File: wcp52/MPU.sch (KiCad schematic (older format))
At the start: 56 parts, among them J6 JLINK, J8 AVR-ICSP, U12 ATSAM4S16CA-AU, U18 ATMEGA32U4-AU-DNP, X2 12MHz

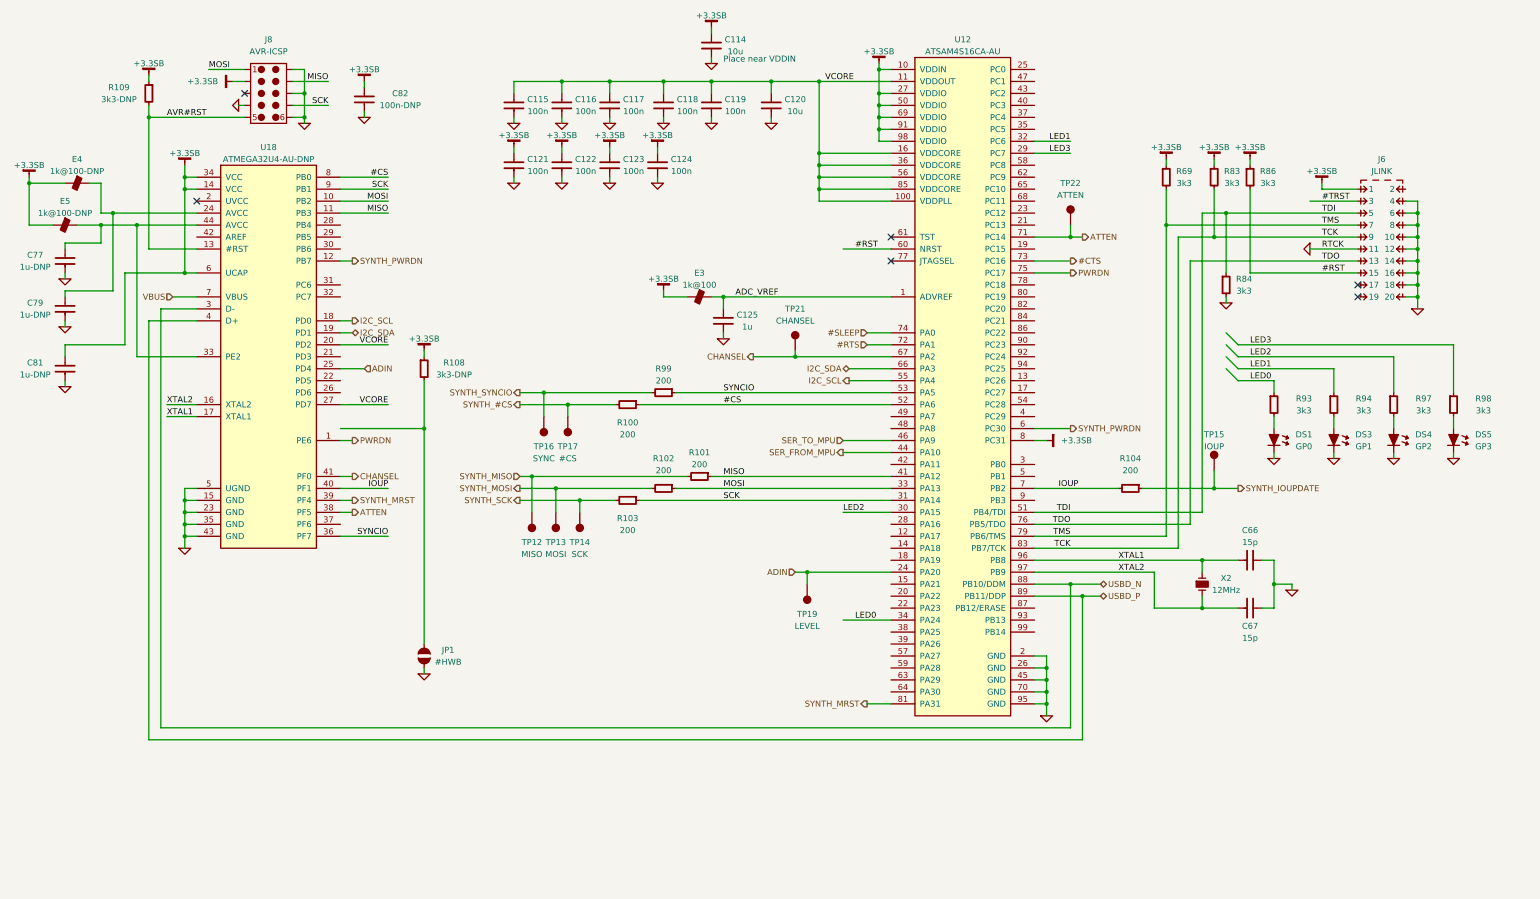
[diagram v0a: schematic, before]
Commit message: Route DDS's SDIO1 to MCUs
Just in case...
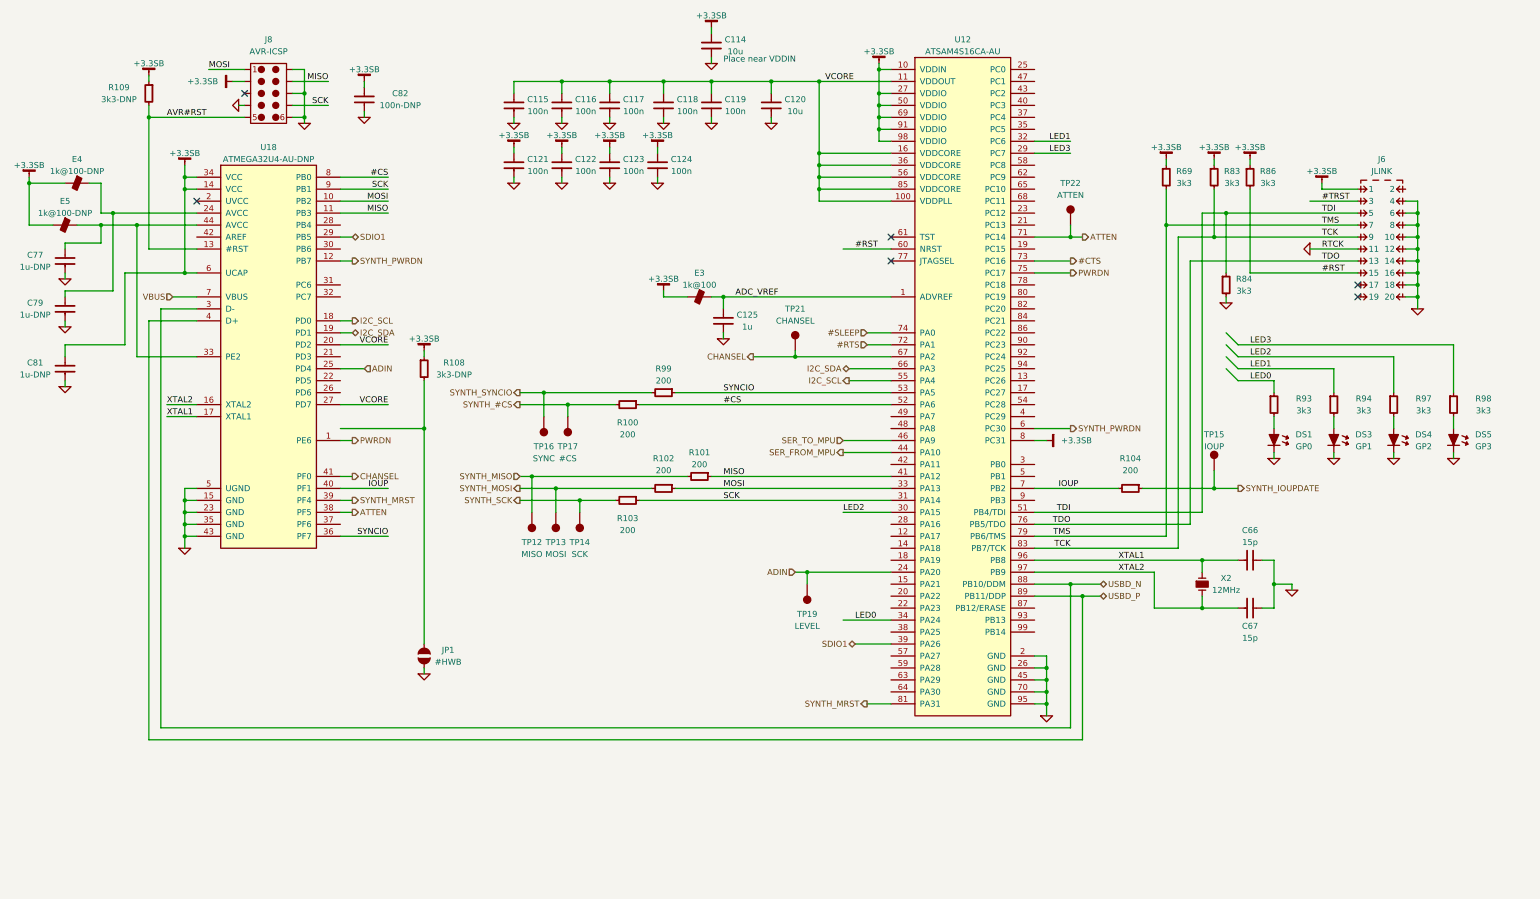
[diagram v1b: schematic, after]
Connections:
- net SDIO1: now reaches U12.39 (PA26)
- net SDIO1: now also U18.29 (PB5)
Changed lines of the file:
@@
 $EndComp
 Wire Wire Line
-	9200 6000 9200 6100
-Wire Wire Line
-	9200 6100 9200 6200
-Wire Wire Line
-	9200 6200 9200 6300
-Wire Wire Line
-	9200 6300 9200 6400
-Wire Wire Line
-	9200 6400 9200 6500
+	9200 6000 9200 6500
 Wire Wire Line
 	9200 6000 9100 6000
@@
 Connection ~ 9200 6400
 Wire Wire Line
-	4750 1200 5150 1200
-Wire Wire Line
-	5150 1200 5550 1200
-Wire Wire Line
-	5550 1200 6000 1200
-Wire Wire Line
-	6000 1200 6400 1200
-Wire Wire Line
-	6400 1200 6900 1200
-Wire Wire Line
-	6900 1200 7300 1200
-Wire Wire Line
-	7300 1200 7900 1200
-Wire Wire Line
-	7300 1200 7300 1800
-Wire Wire Line
-	7300 1800 7300 1900
-Wire Wire Line
-	7300 1900 7300 2000
-Wire Wire Line
-	7300 2000 7300 2100
-Wire Wire Line
-	7300 2100 7300 2200
+	4750 1200 7900 1200
+Wire Wire Line
+	7300 1200 7300 2200
 Wire Wire Line
 	7300 1800 7900 1800
@@
 Connection ~ 7300 2100
 Wire Wire Line
-	7800 1050 7800 1100
-Wire Wire Line
-	7800 1100 7800 1300
-Wire Wire Line
-	7800 1300 7800 1400
-Wire Wire Line
-	7800 1400 7800 1500
-Wire Wire Line
-	7800 1500 7800 1600
-Wire Wire Line
-	7800 1600 7800 1700
+	7800 1050 7800 1700
 Wire Wire Line
 	7800 1700 7900 1700
@@
 	5950 1750 5950 1800
 Wire Wire Line
-	6400 3000 6500 3000
-Wire Wire Line
-	6500 3000 7900 3000
+	6400 3000 7900 3000
 Wire Wire Line
 	6000 2950 6000 3000
@@
 	6500 3350 6500 3300
 Wire Wire Line
-	9100 5200 10500 5200
-Wire Wire Line
-	10500 5200 10800 5200
+	9100 5200 10800 5200
 Wire Wire Line
 	10500 5200 10500 5300
@@
 	10100 5300 10100 5600
 Wire Wire Line
-	10100 5600 10500 5600
-Wire Wire Line
-	10500 5600 10800 5600
+	10100 5600 10800 5600
 Wire Wire Line
 	10500 5600 10500 5500
@@
 	11000 5200 11100 5200
 Wire Wire Line
-	11100 5200 11100 5400
-Wire Wire Line
-	11100 5400 11100 5600
+	11100 5200 11100 5600
 Wire Wire Line
 	11100 5600 11000 5600
@@
 Connection ~ 11100 5400
 Wire Wire Line
-	9100 5400 9400 5400
-Wire Wire Line
-	9400 5400 9650 5400
-Wire Wire Line
-	9100 5500 9500 5500
-Wire Wire Line
-	9500 5500 9650 5500
+	9100 5400 9650 5400
+Wire Wire Line
+	9100 5500 9650 5500
 Wire Wire Line
 	9100 4800 10500 4800
@@
 	7900 4200 7500 4200
 Wire Wire Line
-	12300 2200 12300 2300
-Wire Wire Line
-	12300 2300 12300 2400
-Wire Wire Line
-	12300 2400 12300 2500
-Wire Wire Line
-	12300 2500 12300 2600
-Wire Wire Line
-	12300 2600 12300 2700
-Wire Wire Line
-	12300 2700 12300 2800
-Wire Wire Line
-	12300 2800 12300 2900
-Wire Wire Line
-	12300 2900 12300 3000
-Wire Wire Line
-	12300 3000 12300 3100
+	12300 2200 12300 3100
 Wire Wire Line
 	12300 2200 12200 2200
@@
 	11400 2200 11800 2200
 Wire Wire Line
-	10500 2300 10700 2300
-Wire Wire Line
-	10700 2300 11800 2300
+	10500 2300 11800 2300
 Wire Wire Line
 	10200 2400 11800 2400
 Wire Wire Line
-	10300 2500 10600 2500
-Wire Wire Line
-	10600 2500 11800 2500
+	10300 2500 11800 2500
 Wire Wire Line
 	11400 2600 11800 2600
@@
 	10900 2800 11800 2800
 Wire Wire Line
-	10200 2100 10200 2400
-Wire Wire Line
-	10200 2400 10200 5000
+	10200 2100 10200 5000
 Connection ~ 10200 2400
 Wire Wire Line
@@
 	10900 1850 10900 1900
 Wire Wire Line
-	4800 3900 5200 3900
-Wire Wire Line
-	5200 3900 5600 3900
-Wire Wire Line
-	10000 4600 10600 4600
-Wire Wire Line
-	10600 4600 10800 4600
+	4800 3900 5600 3900
+Wire Wire Line
+	10000 4600 10800 4600
 Wire Wire Line
 	7700 6400 7900 6400
 Wire Wire Line
-	4800 3800 5000 3800
-Wire Wire Line
-	5000 3800 5900 3800
-Wire Wire Line
-	6750 3500 7100 3500
-Wire Wire Line
-	7100 3500 7900 3500
-Wire Wire Line
-	4800 4700 5300 4700
-Wire Wire Line
-	5300 4700 5600 4700
-Wire Wire Line
-	4800 4500 4900 4500
-Wire Wire Line
-	4900 4500 6200 4500
-Wire Wire Line
-	4800 4600 5100 4600
-Wire Wire Line
-	5100 4600 5900 4600
-Wire Wire Line
-	7100 5300 7200 5300
-Wire Wire Line
-	7200 5300 7900 5300
+	4800 3800 5900 3800
+Wire Wire Line
+	6750 3500 7900 3500
+Wire Wire Line
+	4800 4700 5600 4700
+Wire Wire Line
+	4800 4500 6200 4500
+Wire Wire Line
+	4800 4600 5900 4600
+Wire Wire Line
+	7100 5300 7900 5300
 Wire Wire Line
 	7550 3600 7900 3600
@@
 Connection ~ 7200 5300
 Wire Wire Line
-	9100 2500 9400 2500
-Wire Wire Line
-	9400 2500 9500 2500
+	9100 2500 9500 2500
 Wire Wire Line
 	9400 2800 9100 2800
@@
 	2000 2100 2100 2100
 Wire Wire Line
-	2000 1900 2000 2000
-Wire Wire Line
-	2000 2000 2000 2100
-Wire Wire Line
-	2000 2100 2000 2800
+	2000 1900 2000 2800
 Wire Wire Line
 	2100 2000 2000 2000
 Connection ~ 2000 2000
 Wire Wire Line
-	1100 2400 1300 2400
-Wire Wire Line
-	1300 2400 1600 2400
-Wire Wire Line
-	1600 2400 2100 2400
+	1100 2400 2100 2400
 Wire Wire Line
 	700  2400 900  2400
 Wire Wire Line
-	700  2000 700  2050
-Wire Wire Line
-	700  2050 700  2400
+	700  2000 700  2400
 Wire Wire Line
 	1000 2050 700  2050
@@
 	1300 2050 1300 2300
 Wire Wire Line
-	1300 2300 1400 2300
-Wire Wire Line
-	1400 2300 2100 2300
+	1300 2300 2100 2300
 Wire Wire Line
 	1000 2600 1000 2550
@@
 	1500 3400 1500 2800
 Wire Wire Line
-	1500 2800 2000 2800
-Wire Wire Line
-	2000 2800 2100 2800
+	1500 2800 2100 2800
 Wire Wire Line
 	1000 3750 1000 3700
@@
 Connection ~ 9400 5400
 Wire Wire Line
-	2000 4600 2000 4700
-Wire Wire Line
-	2000 4700 2000 4800
-Wire Wire Line
-	2000 4800 2000 4900
-Wire Wire Line
-	2000 4900 2000 5000
-Wire Wire Line
-	2000 5000 2000 5100
+	2000 4600 2000 5100
 Wire Wire Line
 	2000 4600 2100 4600
@@
 	3300 4100 4000 4100
 Wire Wire Line
-	4000 3700 4000 4100
-Wire Wire Line
-	4000 4100 4000 5900
+	4000 3700 4000 5900
 $Comp
 L JUMPER-SOLDER JP1
@@
 	2500 1500 1700 1500
 Wire Wire Line
-	1700 1400 1700 1500
-Wire Wire Line
-	1700 1500 1700 2600
+	1700 1400 1700 2600
 Wire Wire Line
 	1700 2600 2100 2600
@@
 	2900 1100 3000 1100
 Wire Wire Line
-	3000 1100 3000 1300
-Wire Wire Line
-	3000 1300 3000 1500
-Wire Wire Line
-	3000 1500 3000 1550
+	3000 1100 3000 1550
 Wire Wire Line
 	2900 1500 3000 1500
@@
 Wire Wire Line
 	3500 1200 3500 1250
+Text HLabel 7600 5900 0    50   BiDi ~ 0
+SDIO1
+Wire Wire Line
+	7600 5900 7900 5900
+Text HLabel 3400 2500 2    50   BiDi ~ 0
+SDIO1
+Wire Wire Line
+	3400 2500 3300 2500
 $EndSCHEMATC

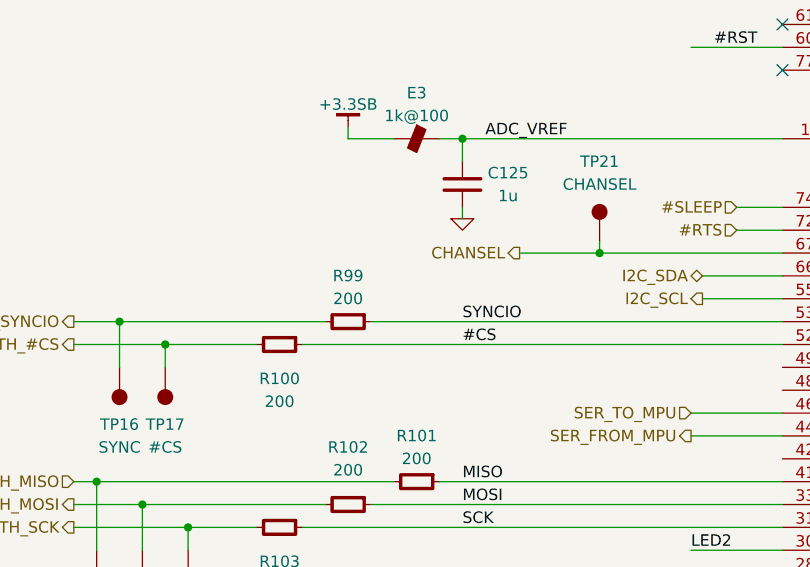
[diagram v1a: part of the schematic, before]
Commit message: Add #CS pullup resistor
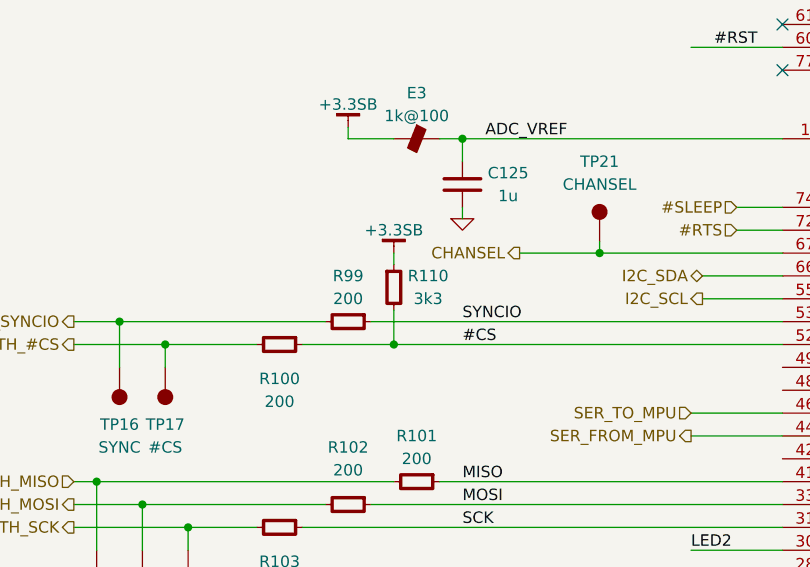
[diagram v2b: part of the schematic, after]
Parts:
- added R110: 3k3, IPC7351-Nominal:RESC1608X50, symbol R-0603
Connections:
- net #CS: now also R110.2
- net +3.3SB: now also R110.1
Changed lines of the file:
@@
 Wire Wire Line
 	3400 2500 3300 2500
+$Comp
+L R-0603 R110
+U 1 1 55011121
+P 6200 3650
+F 0 "R110" H 6350 3700 50  0000 C CNN
+F 1 "3k3" H 6350 3600 50  0000 C CNN
+F 2 "IPC7351-Nominal:RESC1608X50" H 6200 3650 50  0001 C CNN
+F 3 "" H 6200 3700 60  0000 C CNN
+F 4 "Value" H 6200 3650 60  0001 C CNN "Manuf"
+F 5 "RES SMD 3.3k 5% [0603]" H 6950 4200 60  0001 C CNN "BOM"
+	1    6200 3650
+	1    0    0    -1
+$EndComp
+Wire Wire Line
+	6200 3750 6200 3900
+Connection ~ 6200 3900
+$Comp
+L +3.3SB #PWR0265
+U 1 1 550116AB
+P 6200 3500
+F 0 "#PWR0265" H 6200 3550 30  0001 C CNN
+F 1 "+3.3SB" H 6200 3600 50  0000 C CNN
+F 2 "" H 6200 3500 60  0000 C CNN
+F 3 "" H 6200 3500 60  0000 C CNN
+	1    6200 3500
+	1    0    0    -1
+$EndComp
+Wire Wire Line
+	6200 3500 6200 3550
 $EndSCHEMATC

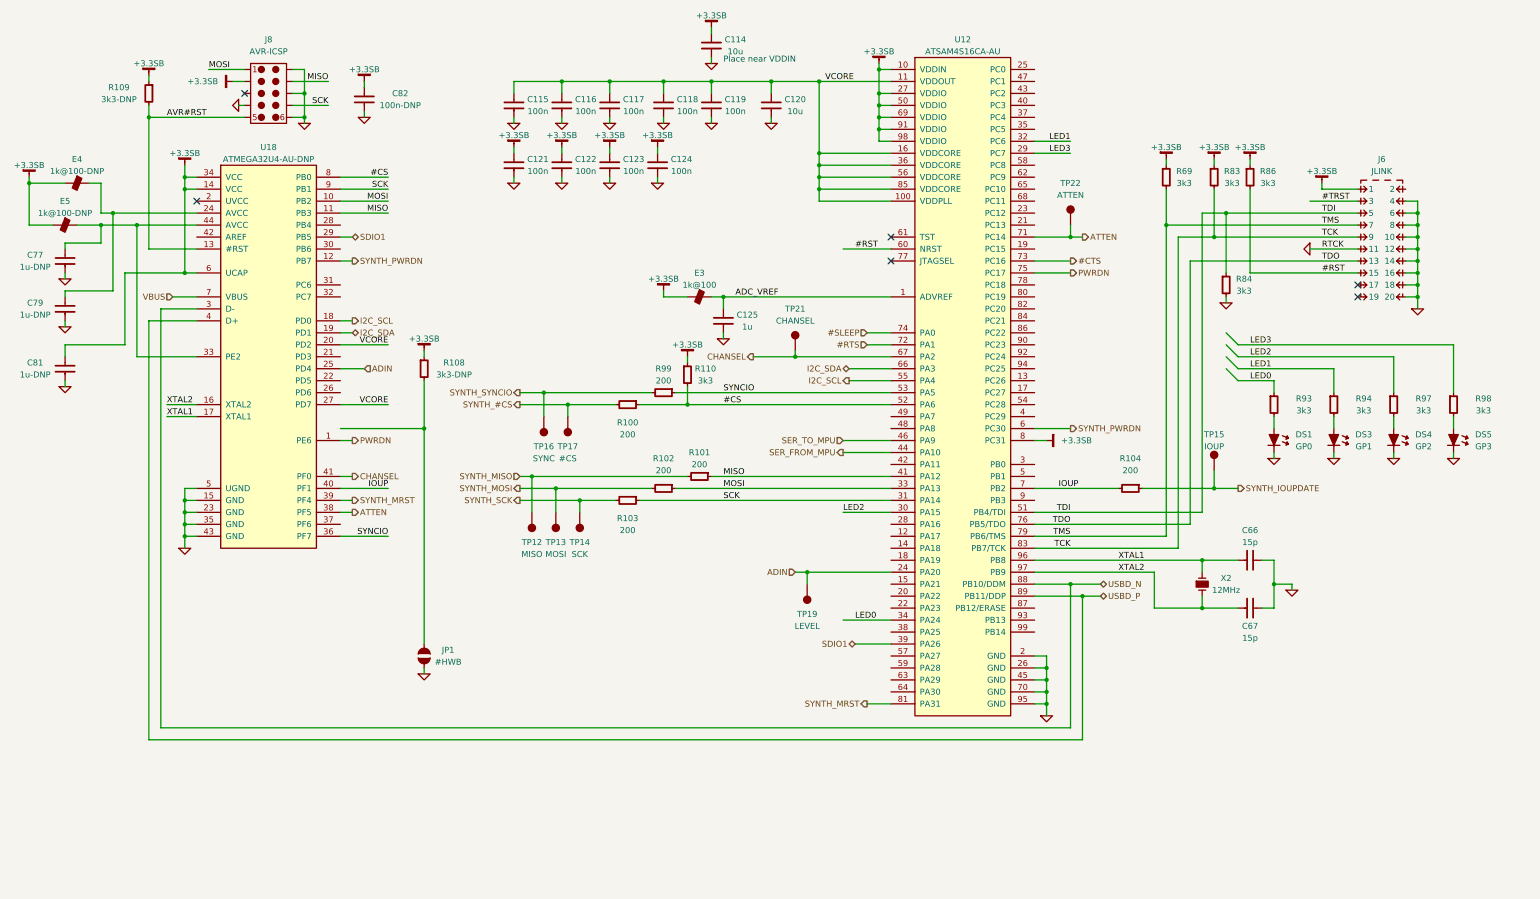
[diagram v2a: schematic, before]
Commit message: Route UART to alt MCU
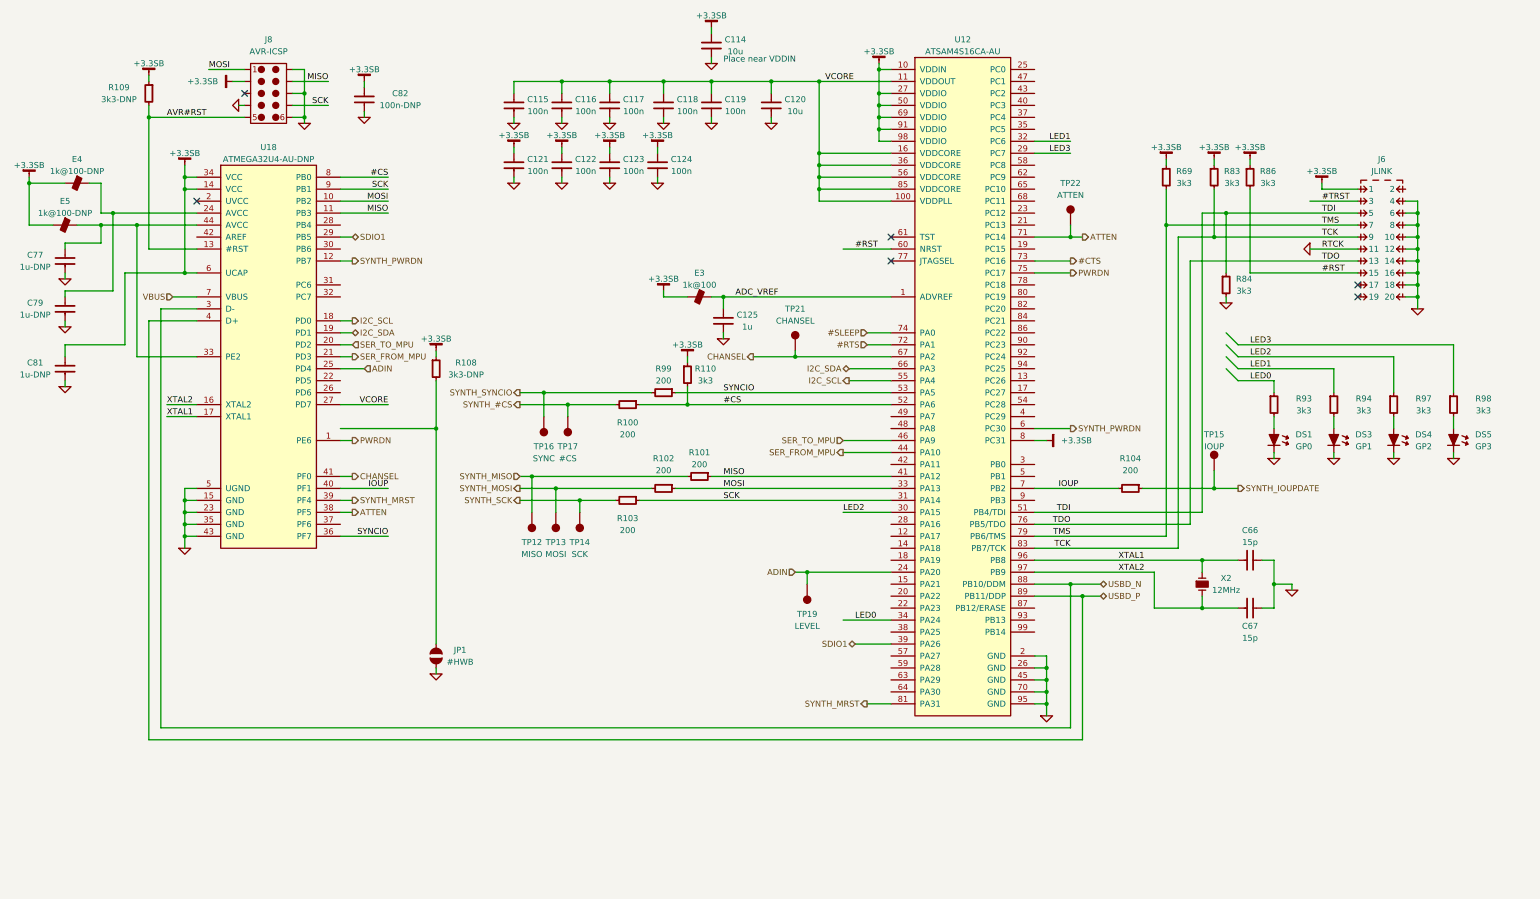
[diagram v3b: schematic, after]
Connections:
- net SER_FROM_MPU: now also U18.21 (PD3)
- net SER_TO_MPU: now also U18.20 (PD2)
- net VCORE: no longer U18.20 (PD2)
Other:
- moved on the sheet: JP1, R108
